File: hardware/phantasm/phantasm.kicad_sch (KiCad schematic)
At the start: 28 parts, among them J1 +5V IN ~1A, J2 LED sig DI/CI/SIG_GND, J3A SYNC in, J3B SYNC out, J4 debug, U1 74AHCT125

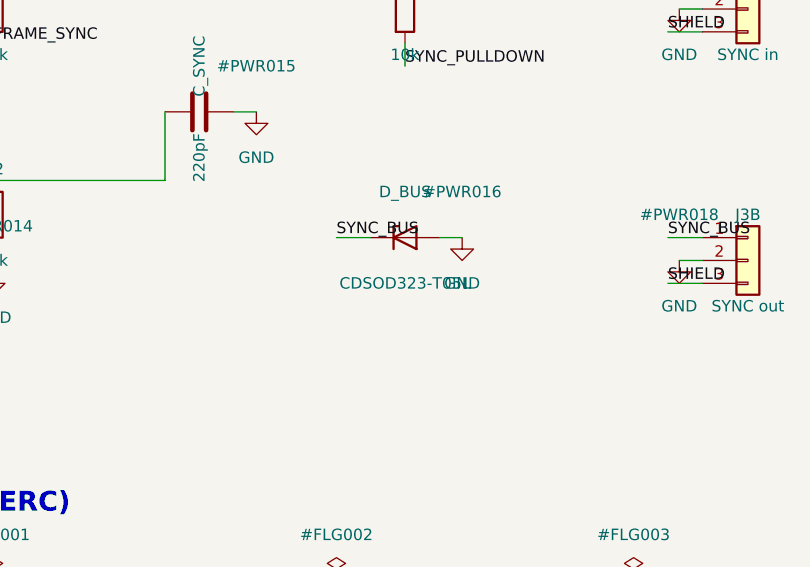
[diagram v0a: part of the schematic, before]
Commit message: hardware: raise sync TVS standoff above the drive rail (finding 317)
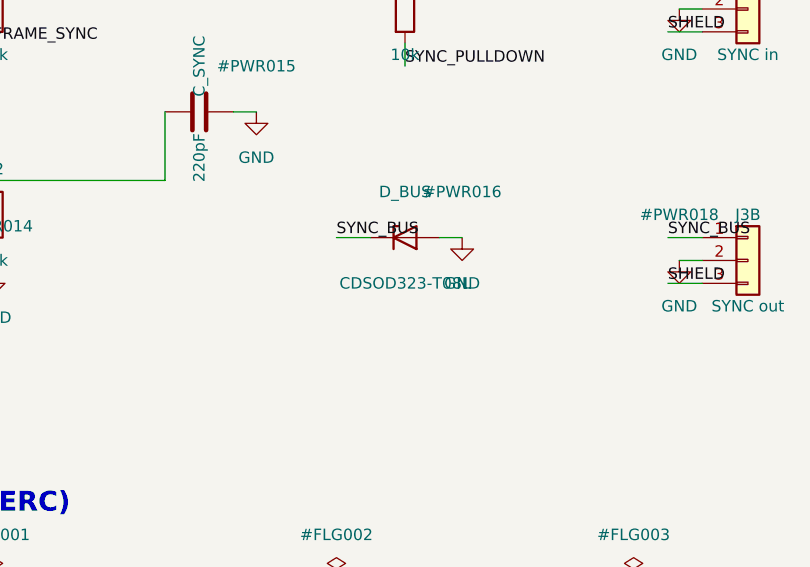
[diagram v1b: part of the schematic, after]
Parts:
- D_BUS: value CDSOD323-T05L -> CDSOD323-T08L
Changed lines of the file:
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@@
 			(effects (font (size 1.27 1.27)))
 		)
-		(property "Value" "CDSOD323-T05L"
+		(property "Value" "CDSOD323-T08L"
 			(at 292.1 236.22 0)
 			(effects (font (size 1.27 1.27)))

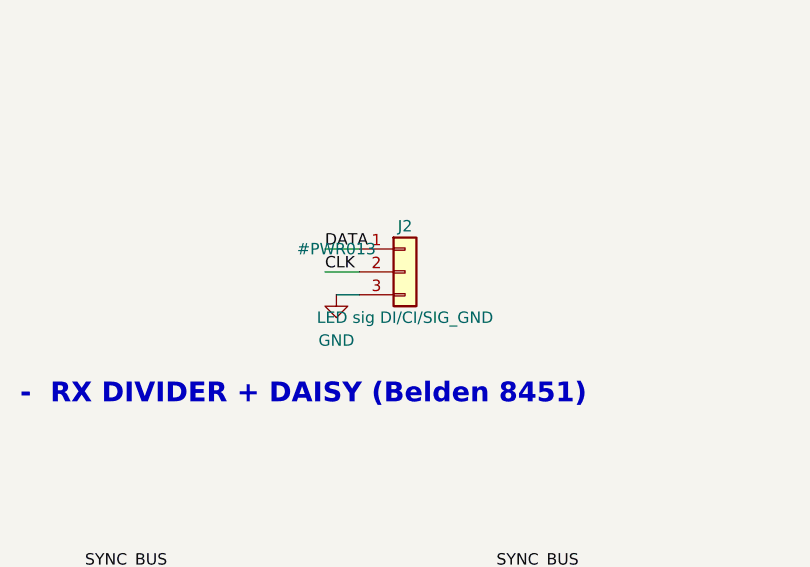
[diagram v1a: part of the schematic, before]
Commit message: hardware: place the strip return between data and clock (finding 318)
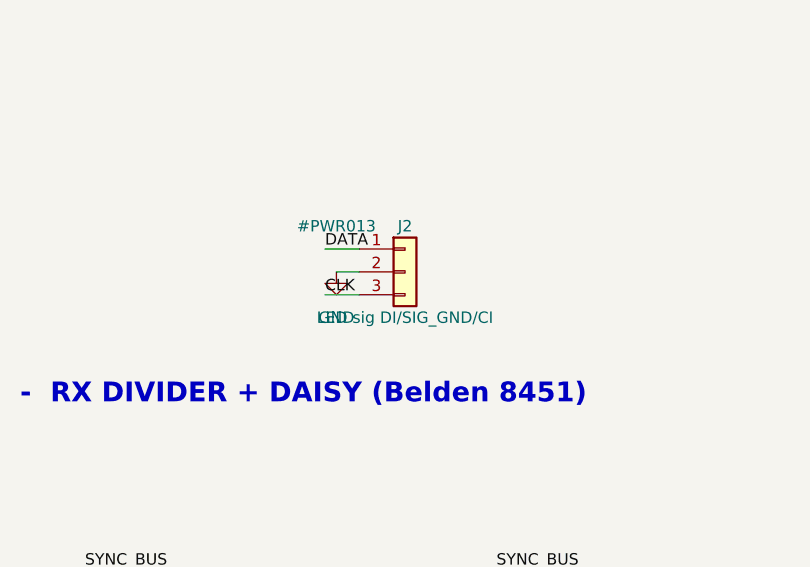
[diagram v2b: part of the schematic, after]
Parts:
- J2: value LED sig DI/CI/SIG_GND -> LED sig DI/SIG_GND/CI
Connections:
- net CLK: now also J2.3 (Pin_3); no longer J2.2 (Pin_2)
- net GND: now also J2.2 (Pin_2); no longer J2.3 (Pin_3)
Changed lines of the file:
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@@
 	)
 	(wire
-		(pts (xy 276.86 165.1) (xy 273.05 165.1))
-		(stroke (width 0) (type default))
-	)
-	(wire
-		(pts (xy 276.86 167.64) (xy 274.32 167.64))
+		(pts (xy 276.86 167.64) (xy 273.05 167.64))
+		(stroke (width 0) (type default))
+	)
+	(wire
+		(pts (xy 276.86 165.1) (xy 274.32 165.1))
 		(stroke (width 0) (type default))
 	)
@@
 	)
 	(label "CLK"
-		(at 273.05 165.1 0)
+		(at 273.05 167.64 0)
 		(effects (font (size 1.27 1.27)) (justify left bottom))
 	)
@@
 			(effects (font (size 1.27 1.27)))
 		)
-		(property "Value" "LED sig DI/CI/SIG_GND"
+		(property "Value" "LED sig DI/SIG_GND/CI"
 			(at 281.94 170.18 0)
 			(effects (font (size 1.27 1.27)))
@@
 	(symbol
 		(lib_id "power:GND")
-		(at 274.32 167.64 0)
+		(at 274.32 165.1 0)
 		(unit 1)
 		(exclude_from_sim no)
@@
 		(dnp no)
 		(property "Reference" "#PWR013"
-			(at 274.32 162.56 0)
+			(at 274.32 160.02 0)
 			(effects (font (size 1.27 1.27)))
 		)
 		(property "Value" "GND"
+			(at 274.32 170.18 0)
+			(effects (font (size 1.27 1.27)))
+		)
+		(property "Footprint" ""
 			(at 274.32 172.72 0)
-			(effects (font (size 1.27 1.27)))
-		)
-		(property "Footprint" ""
-			(at 274.32 175.26 0)
-			(effects (font (size 1.27 1.27)) (hide yes))
-		)
-		(property "Datasheet" ""
-			(at 274.32 167.64 0)
-			(effects (font (size 1.27 1.27)) (hide yes))
-		)
+			(effects (font (size 1.27 1.27)) (hide yes))
+		)
+		(property "Datasheet" ""
+			(at 274.32 165.1 0)
+			(effects (font (size 1.27 1.27)) (hide yes))
+		)

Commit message: pcb: exclude solder jumpers from schematic BOM (finding 150)
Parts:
- JP_ID0, JP_ID1, JP_ID2, JP_SHLD: now left out of the parts list
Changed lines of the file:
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@@
 		(unit 1)
 		(exclude_from_sim no)
-		(in_bom yes)
+		(in_bom no)
 		(on_board yes)
 		(dnp no)
@@
 		(unit 1)
 		(exclude_from_sim no)
-		(in_bom yes)
+		(in_bom no)
 		(on_board yes)
 		(dnp no)
@@
 		(unit 1)
 		(exclude_from_sim no)
-		(in_bom yes)
+		(in_bom no)
 		(on_board yes)
 		(dnp no)
@@
 		(unit 1)
 		(exclude_from_sim no)
-		(in_bom yes)
-		(on_board yes)
-		(dnp no)
+		(in_bom no)
+		(on_board yes)
+		(dnp no)
